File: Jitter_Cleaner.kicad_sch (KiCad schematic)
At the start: 33 parts, among them J17 MMCX, J20 MMCX, T1 TCM2-43X, T3 TCM2-43X, U18 SI5394, U23 74AVC4T245, U26 74LVC8T245, Y1 CX3225SB48000D0FPJC1

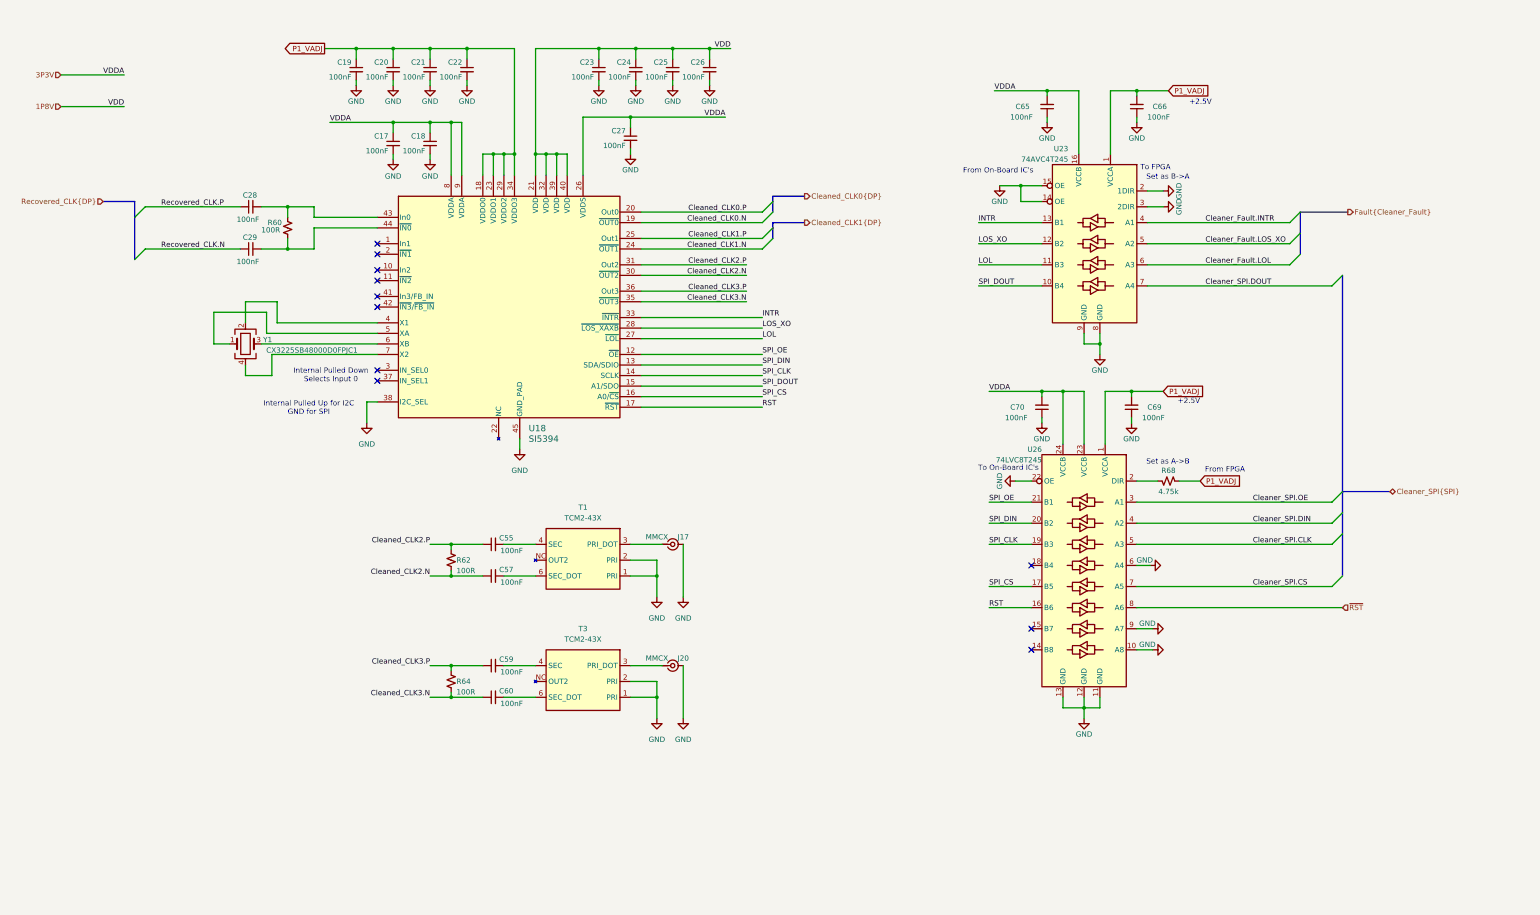
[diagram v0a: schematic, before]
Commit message: Completed Schematic
Completed Schematic Draft
- Includes careful pin mapping to avoid conflicts with other firmwares
- Roughed out LCB layout high speed traces, and FMC breakouts.

Layout and BOM are still WIP
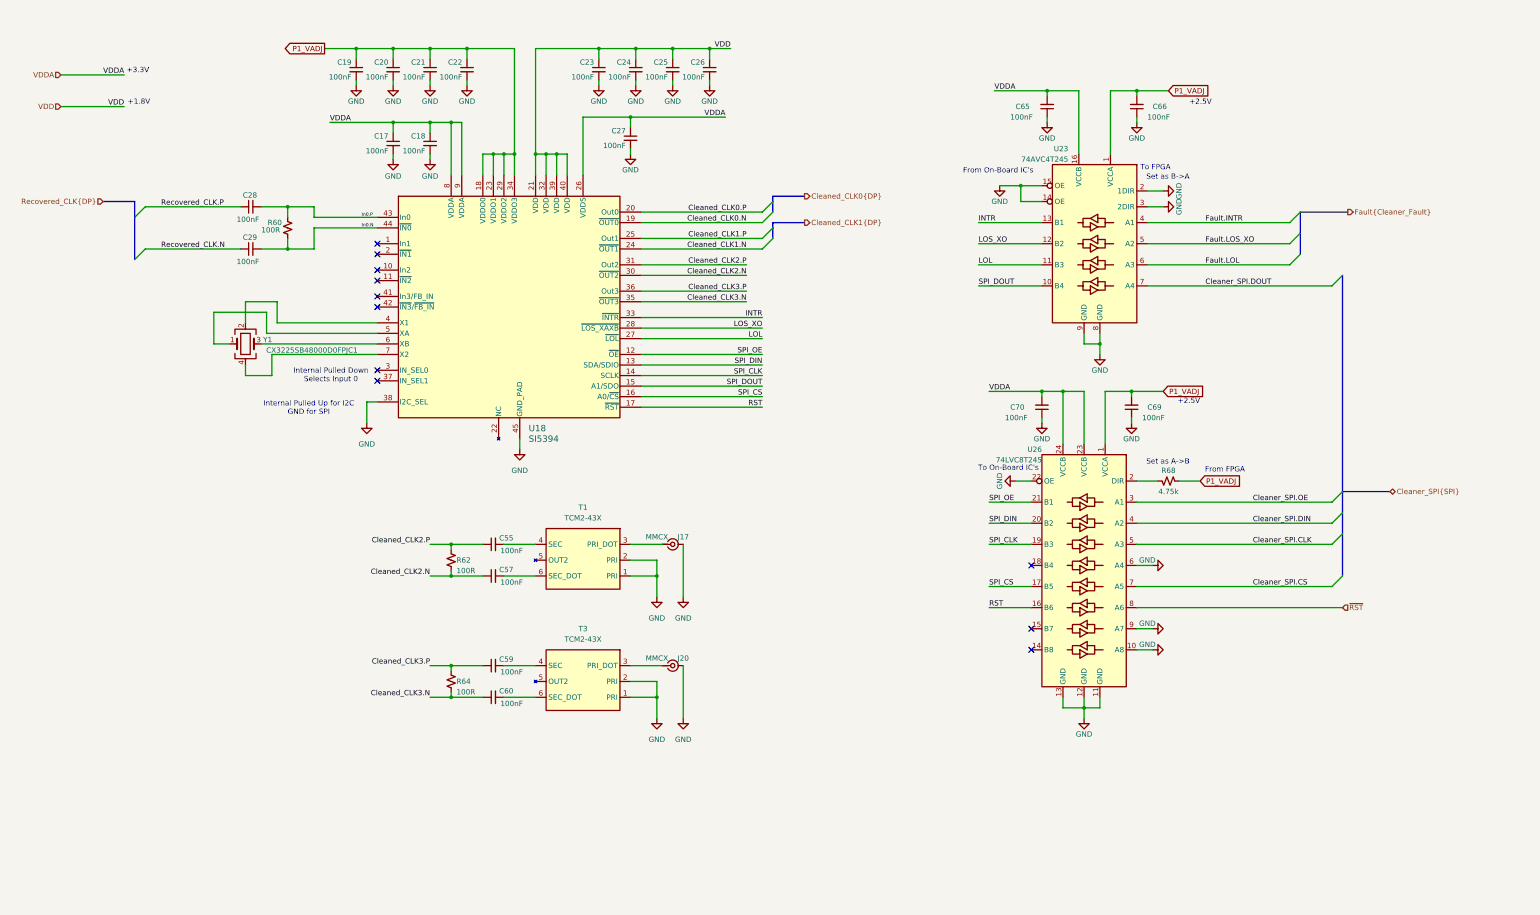
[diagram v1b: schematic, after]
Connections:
- net In0.P: now reaches C28.2, R60.1, U18.43 (In0)
- net In0.N: now reaches C29.2, R60.2, U18.44 (~{IN0})
- net 1P8V renamed VDD
- net 3P3V renamed VDDA
- net Cleaner_Fault.INTR renamed Fault.INTR
- net Cleaner_Fault.LOL renamed Fault.LOL
- net Cleaner_Fault.LOS_XO renamed Fault.LOS_XO
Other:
- note added: "+1.8V"
- note added: "+3.3V"

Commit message: Updated Schematic and continued layout work
schematic:
- Added 0ohm resistor in power section
- Added pull up and down to digital lines to define powerup behavior
- Added some power filter between jitter cleaner IC's

layout:
-Overall Still WIP
-defined all needed fmc pins
-started layout of critical clock signals and connector locations.
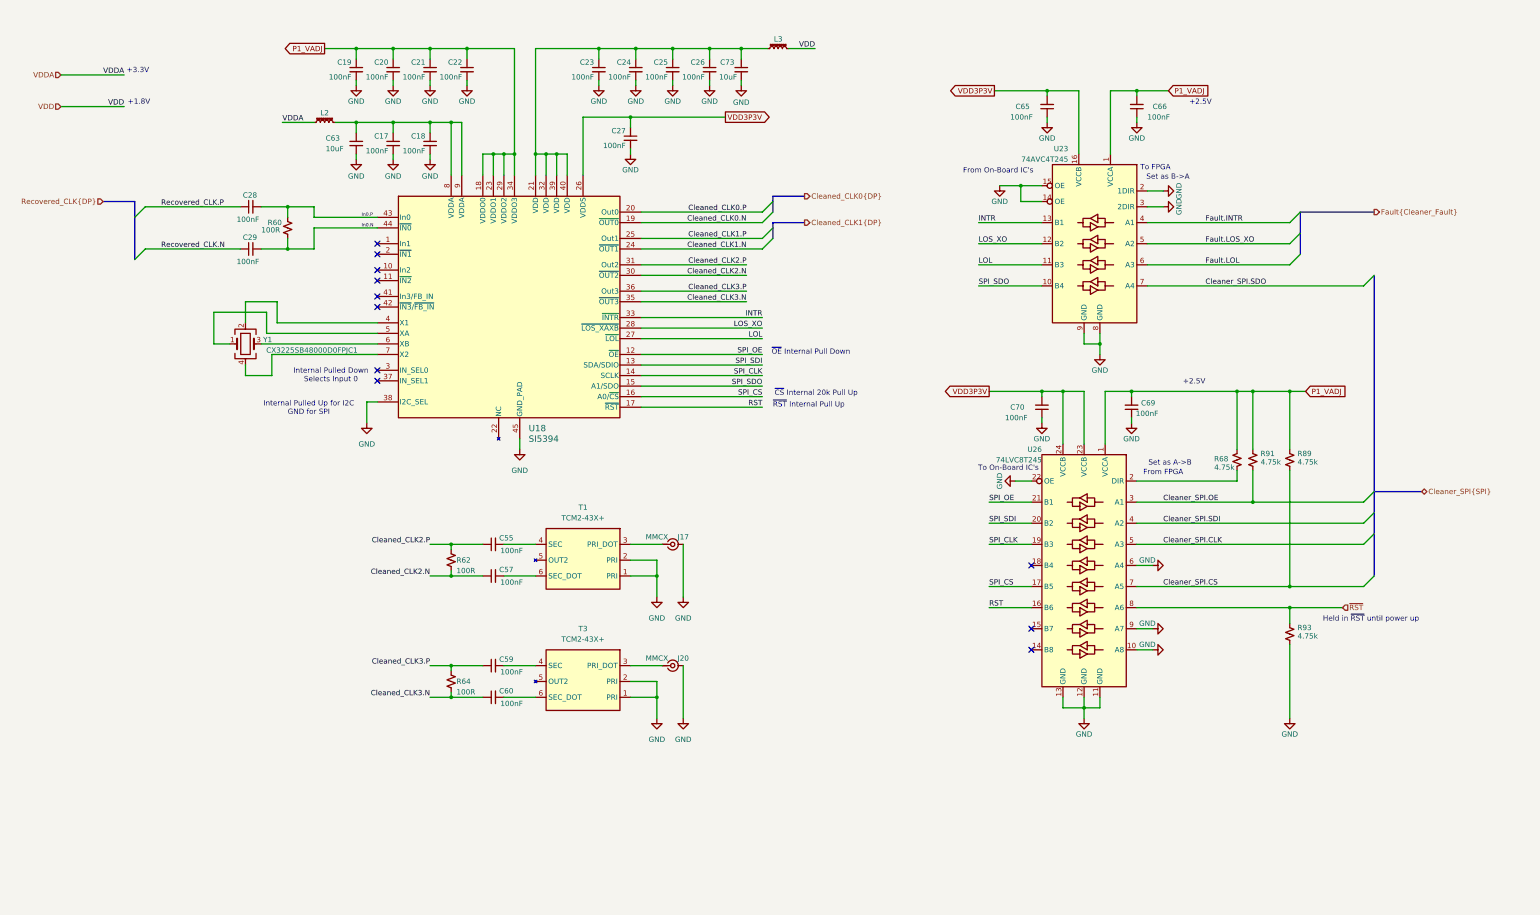
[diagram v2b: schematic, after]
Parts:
- added C63, C73: 10uF, Capacitor_SMD:C_0805_2012Metric, symbol Device:C_Small
- added L2, L3: 60R@100Mhz; 3.5A, Inductor_SMD:L_0805_2012Metric, symbol Device:L_Ferrite_Small
- added R89, R91, R93: 4.75k, Resistor_SMD:R_0603_1608Metric, symbol Device:R_Small_US
- T1, T3: value TCM2-43X -> TCM2-43X+; MPN TCM2-43X -> TCM2-43X+
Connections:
- net Cleaner_SPI.CS: now also R89.1
- net Cleaner_SPI.OE: now also R91.1
- net GND: now also C63.2, C73.2, R93.1
- net P1_VADJ: now also R89.2, R91.2
- net VDD: now also L3.2; no longer C23.1, C24.1, C25.1, C26.1, U18.21 (VDD), U18.32 (VDD), U18.39 (VDD), U18.40 (VDD)
- net VDDA: now also L2.1; no longer C17.1, C18.1, C27.1, C65.2, C70.2, U18.26 (VDDS), U18.8 (VDDA), U18.9 (VDDA), U23.16 (VCCB), U26.23 (VCCB), U26.24 (VCCB)
- net ~{RST}: now also R93.2
- net Cleaner_SPI.DIN renamed Cleaner_SPI.SDI
- net Cleaner_SPI.DOUT renamed Cleaner_SPI.SDO
- net SPI_DIN renamed SPI_SDI
- net SPI_DOUT renamed SPI_SDO
- new net: C23.1, C24.1, C25.1, C26.1, C73.1, L3.1, U18.21 (VDD), U18.32 (VDD), U18.39 (VDD), U18.40 (VDD)
- new net: C17.1, C18.1, C63.1, L2.2, U18.8 (VDDA), U18.9 (VDDA)
- new net VDD3P3V: C27.1, C65.2, C70.2, U18.26 (VDDS), U23.16 (VCCB), U26.23 (VCCB), U26.24 (VCCB)
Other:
- note added: "Held in ~{RST} until power up"
- note added: "~{CS} Internal 20k Pull Up"
- note added: "~{OE} Internal Pull Down"
- note added: "~{RST} Internal Pull Up"
- moved on the sheet: R68

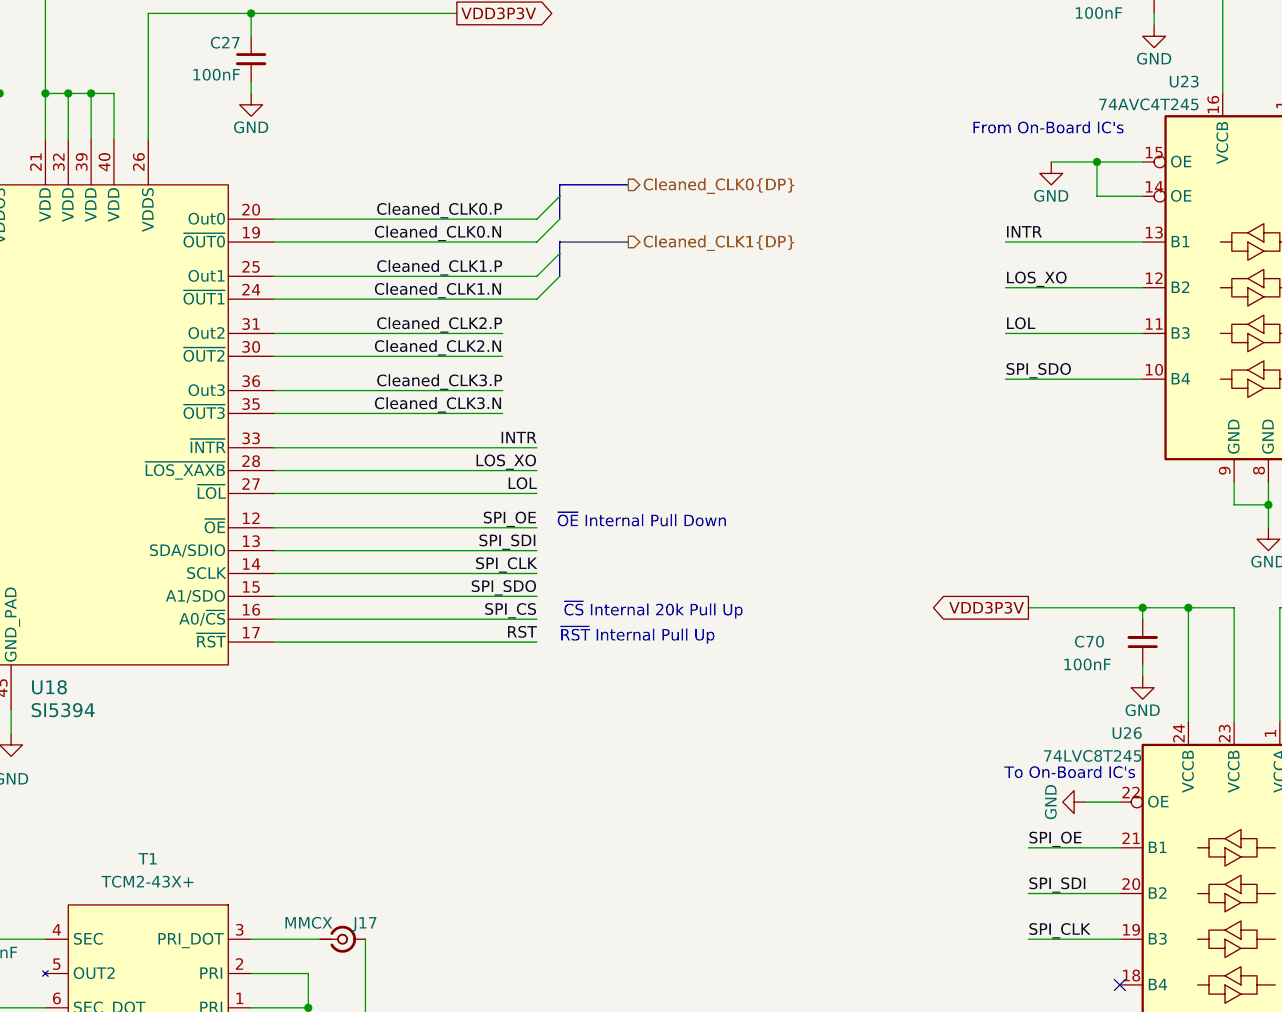
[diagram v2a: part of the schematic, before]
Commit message: Revised Si5394 part and schematic changes
- Revised Si5394 part
- Changed OE pin connection on Si5394
- Removed OE from SPI group
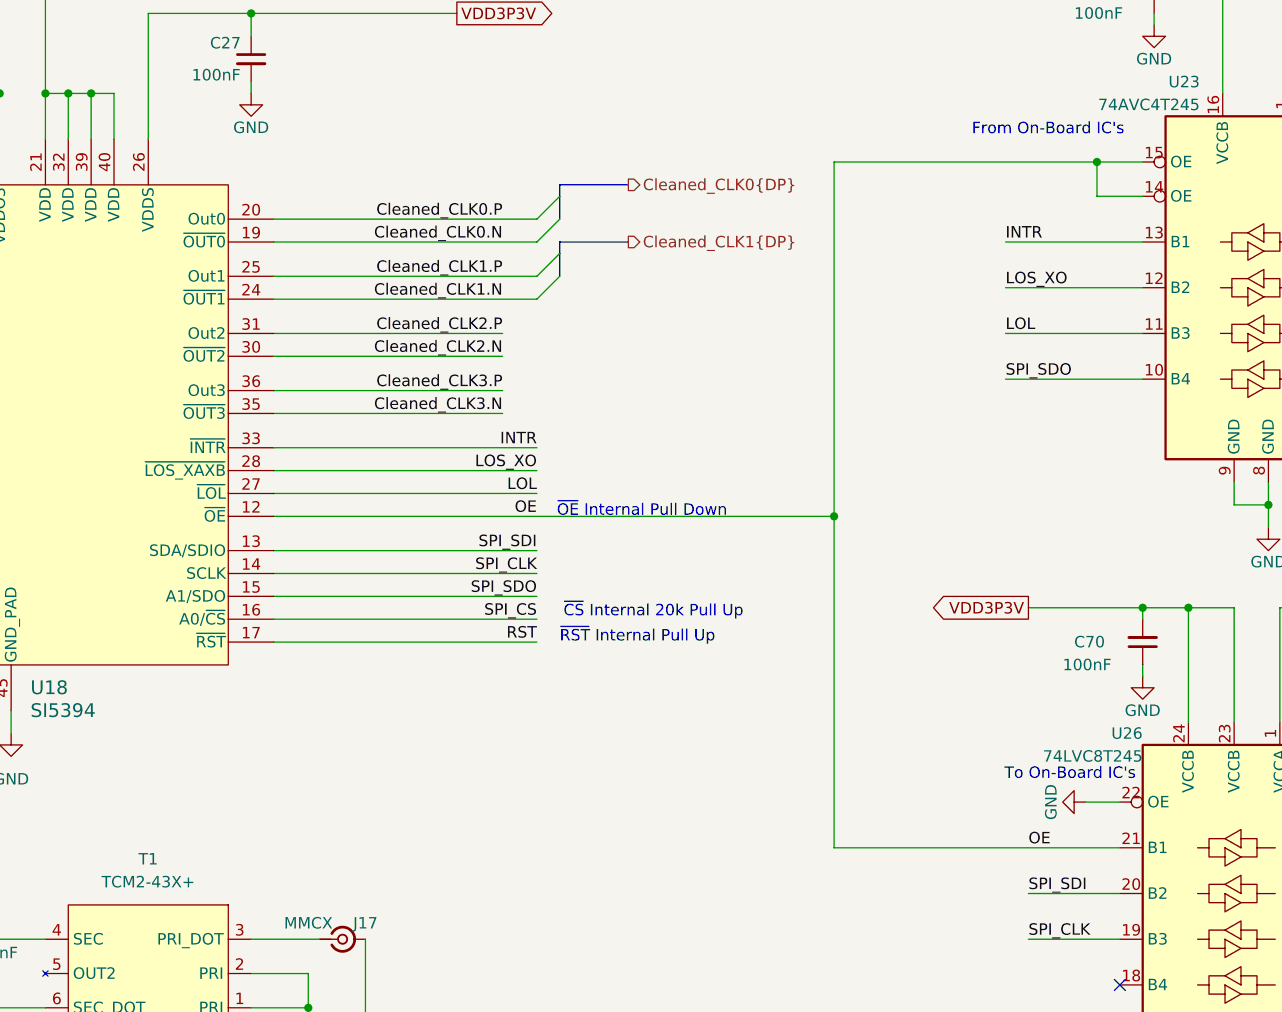
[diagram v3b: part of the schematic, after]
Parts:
- U18: footprint Package_DFN_QFN:QFN-44-1EP_7x7mm_P0.5mm_EP5.2x5.2mm -> rf-input-fmc:QFN-44-1EP_7x7mm_P0.5mm_EP5.2x5.2mm_ThermalVias
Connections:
- net GND: no longer U23.14 (OE), U23.15 (OE)
- net SPI_OE renamed OE
- net OE: now also U23.14 (OE), U23.15 (OE)
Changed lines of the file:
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@@
 	(text "~{OE} Internal Pull Down\n\n"
 		(exclude_from_sim no)
-		(at 225.044 122.428 0)
+		(at 225.044 121.158 0)
 		(effects
 			(font
@@
 	)
 	(junction
+		(at 246.38 120.65)
+		(diameter 0)
+		(color 0 0 0 0)
+	)
+	(junction
 		(at 115.57 48.26)
 		(diameter 0)
@@
 	(wire
 		(pts
-			(xy 275.59 81.28) (xy 270.51 81.28)
-		)
-		(stroke
-			(width 0)
-			(type default)
-		)
-	)
-	(wire
-		(pts
 			(xy 278.13 162.56) (xy 267.97 162.56)
 		)
@@
 	(wire
 		(pts
-			(xy 278.13 157.48) (xy 267.97 157.48)
+			(xy 246.38 157.48) (xy 278.13 157.48)
 		)
 		(stroke
@@
 	(wire
 		(pts
+			(xy 246.38 81.28) (xy 275.59 81.28)
+		)
+		(stroke
+			(width 0)
+			(type default)
+		)
+	)
+	(wire
+		(pts
 			(xy 148.59 73.66) (xy 148.59 78.74)
 		)
@@
 	(wire
 		(pts
-			(xy 184.15 121.92) (xy 213.36 121.92)
+			(xy 184.15 120.65) (xy 246.38 120.65)
 		)
 		(stroke
@@
 	(wire
 		(pts
+			(xy 246.38 120.65) (xy 246.38 157.48)
+		)
+		(stroke
+			(width 0)
+			(type default)
+		)
+	)
+	(wire
+		(pts
 			(xy 280.67 81.28) (xy 275.59 81.28)
 		)
@@
 	(wire
 		(pts
+			(xy 246.38 81.28) (xy 246.38 120.65)
+		)
+		(stroke
+			(width 0)
+			(type default)
+		)
+	)
+	(wire
+		(pts
 			(xy 278.13 152.4) (xy 274.32 152.4)
 		)
@@
 		)
 	)
-	(label "SPI_OE"
+	(label "OE"
 		(at 267.97 157.48 0)
 		(effects
@@
 		)
 	)
-	(label "SPI_OE"
-		(at 213.36 121.92 180)
+	(label "OE"
+		(at 213.36 120.65 180)
 		(effects
 			(font
@@
 			)
 		)
-		(property "Footprint" "Package_DFN_QFN:QFN-44-1EP_7x7mm_P0.5mm_EP5.2x5.2mm"
+		(property "Footprint" "rf-input-fmc:QFN-44-1EP_7x7mm_P0.5mm_EP5.2x5.2mm_ThermalVias"
 			(at 135.636 128.27 0)
 			(effects
@@
 			)
 		)
-		(property "Datasheet" ""
+		(property "Datasheet" "https://www.skyworksinc.com/-/media/SkyWorks/SL/documents/public/data-sheets/si5395-94-92-a-datasheet.pdf"
 			(at 134.62 129.794 0)
 			(effects
@@
 			)
 		)
-		(property "Datasheet" ""
+		(property "Datasheet" "https://www.minicircuits.com/pdfs/TCM2-43X+.pdf"
 			(at 179.07 163.83 0)
 			(effects
@@
 			)
 		)
-		(property "Datasheet" ""
+		(property "Datasheet" "https://www.ti.com/lit/ds/symlink/sn74lvc8t245.pdf"
 			(at 300.99 139.7 0)
 			(effects
@@
 			)
 		)
-		(property "Datasheet" ""
+		(property "Datasheet" "https://www.minicircuits.com/pdfs/TCM2-43X+.pdf"
 			(at 179.07 193.04 0)
 			(effects
@@
 			)
 		)
-		(property "Datasheet" "~"
+		(property "Datasheet" "https://mm.digikey.com/Volume0/opasdata/d220001/medias/docus/1917/CX3225SB48000D0FPJC1.pdf"
 			(at 88.9 119.38 0)
 			(effects
@@
 			)
 		)
-		(property "Datasheet" ""
+		(property "Datasheet" "https://www.ti.com/lit/ds/symlink/sn74avc4t245.pdf"
 			(at 303.53 76.2 0)
 			(effects
@@
 					(unit 1)
 				)
-			)
-		)
-	)
-	(symbol
-		(lib_id "power:GND")
-		(at 270.51 81.28 0)
-		(mirror y)
-		(unit 1)
-		(exclude_from_sim no)
-		(in_bom yes)
-		(on_board yes)
-		(dnp no)
-		(property "Reference" "#PWR0110"
-			(at 270.51 87.63 0)
-			(effects
-				(font
-					(size 1.27 1.27)
-				)
-				(hide yes)
-			)
-		)
-		(property "Value" "GND"
-			(at 270.51 85.09 0)
-			(effects
-				(font
-					(size 1.27 1.27)
-				)
-			)
-		)
-		(property "Footprint" ""
-			(at 270.51 81.28 0)
-			(effects
-				(font
-					(size 1.27 1.27)
-				)
-				(hide yes)
-			)
-		)
-		(property "Datasheet" ""
-			(at 270.51 81.28 0)
-			(effects
-				(font
-					(size 1.27 1.27)
-				)
-				(hide yes)
-			)
-		)
-		(property "Description" ""
-			(at 270.51 81.28 0)
-			(effects
-				(font
-					(size 1.27 1.27)
-				)
-				(hide yes)
-			)
-		)
-		(pin "1"
-		)
-		(instances
-			(project "evr-fmc"
-				(path "/1719e569-47c8-4fa0-8523-9c9686ef0dba/51b6ba02-2a45-47f9-920d-b1129f765b02"
-					(reference "#PWR0118")
-					(unit 1)
-				)
-				(path "/1719e569-47c8-4fa0-8523-9c9686ef0dba/72a6e05f-9d23-47d7-93ac-d48e996d2022"
-					(reference "#PWR0110")
-					(unit 1)
-				)
